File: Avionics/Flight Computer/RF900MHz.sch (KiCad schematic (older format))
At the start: 51 parts, among them J4 734120110, U1 CC1310F128RGZR, U2 CC1190RGVR, Y3 XRCGB24M000F2P00R0

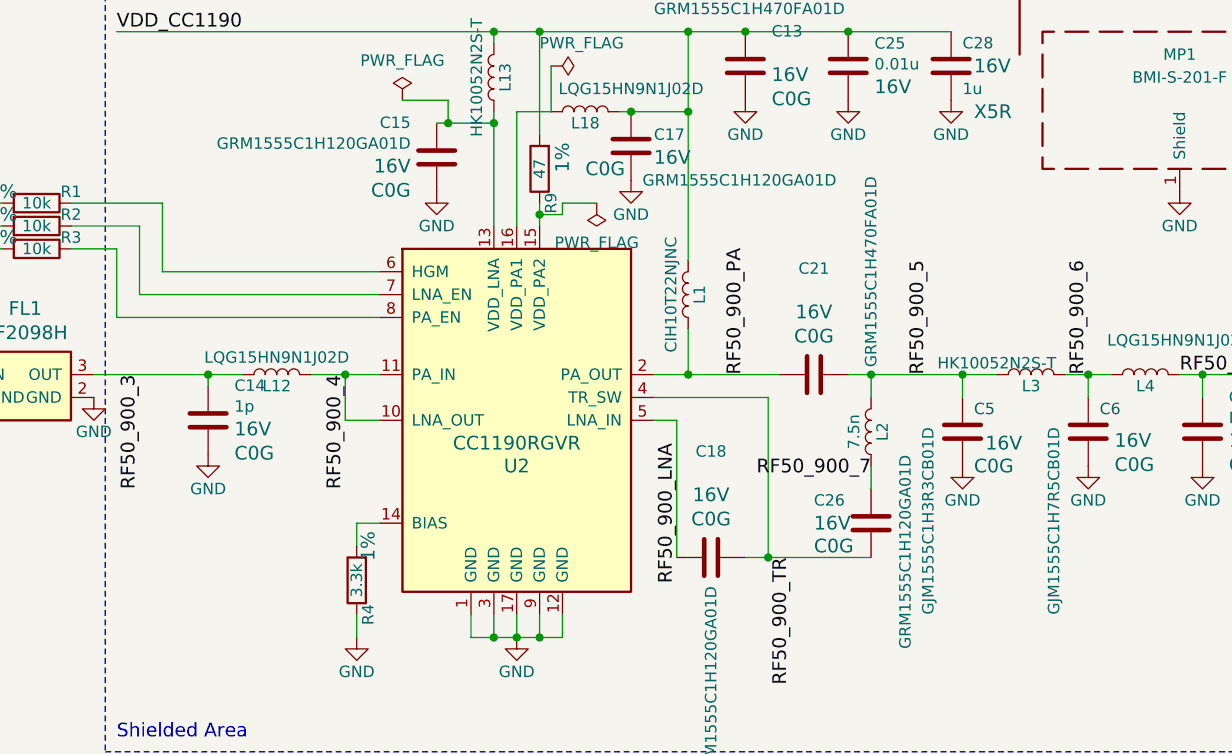
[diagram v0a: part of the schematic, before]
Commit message: Rebuilt output files and generated a few BOM fixes.
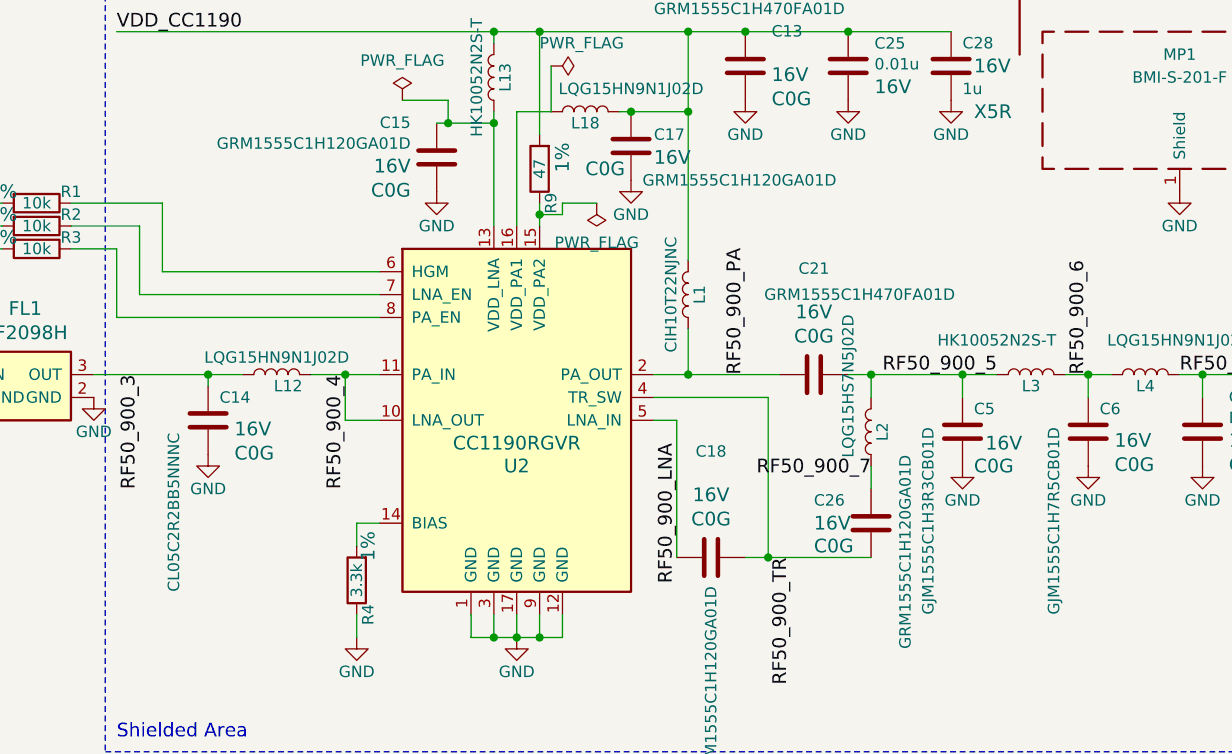
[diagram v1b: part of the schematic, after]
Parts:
- C14: value 1p -> CL05C2R2BB5NNNC
- L2: value 7.5n -> LQG15HS7N5J02D
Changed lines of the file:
@@
 P 8600 2550
 F 0 "L2" V 8550 2550 50  0000 C CNN
-F 1 "7.5n" V 8675 2550 50  0000 C CNN
+F 1 "LQG15HS7N5J02D" V 8700 2350 50  0000 C CNN
 F 2 "Inductors_SMD:L_0402" H 8600 2550 50  0001 C CNN
 F 3 "" H 8600 2550 50  0001 C CNN
@@
 P 9300 2300
 F 0 "L3" V 9250 2300 50  0000 C CNN
-F 1 "HK10052N2S-T" V 9350 2450 50  0000 C CNN
+F 1 "HK10052N2S-T" V 9450 2450 50  0000 C CNN
 F 2 "Inductors_SMD:L_0402" H 9300 2300 50  0001 C CNN
 F 3 "" H 9300 2300 50  0001 C CNN
@@
 U 1 1 58B31E99
 P 6000 2300
-F 0 "L12" V 5950 2300 50  0000 C CNN
+F 0 "L12" V 5950 2250 50  0000 C CNN
 F 1 "LQG15HN9N1J02D" V 6075 2300 50  0000 C CNN
 F 2 "Inductors_SMD:L_0402" H 6000 2300 50  0001 C CNN
@@
 U 1 1 58B4147C
 P 5700 2500
-F 0 "C14" H 5585 2348 50  0000 R CNN
-F 1 "1p" H 5585 2439 50  0000 R CNN
+F 0 "C14" H 5650 2400 50  0000 R CNN
+F 1 "CL05C2R2BB5NNNC" V 5850 3250 50  0000 R CNN
 F 2 "Capacitors_SMD:C_0402" H 988 1050 50  0001 C CNN
 F 3 "" H 950 1200 50  0001 C CNN
@@
 P 8350 2300
 F 0 "C21" V 8814 2300 50  0000 C CNN
-F 1 "GRM1555C1H470FA01D" H 8800 2050 50  0000 C CNN
+F 1 "GRM1555C1H470FA01D" V 8700 2100 50  0000 C CNN
 F 2 "Capacitors_SMD:C_0402" H 3638 850 50  0001 C CNN
 F 3 "" H 3600 1000 50  0001 C CNN
@@
 Text Label 8250 3100 3    60   ~ 0
 RF50_900_TR
-Text Label 8850 2300 1    60   ~ 0
+Text Label 8650 2300 0    60   ~ 0
 RF50_900_5
 Text Label 9550 2300 1    60   ~ 0

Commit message: Updated more manufacturing part numbers for macrofab compatibility.
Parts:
- D6: value LED-0603-RED -> MF-LED-0603-RED
- J4: value 734120110 -> 0734120110
- L15: value BLM18HE152SN1 -> BLM18HE152SN1D
- R4: value 3.3k -> RC0402FR-073K3L
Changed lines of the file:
@@
 P 10900 2300
 F 0 "J4" H 10910 2420 50  0000 C CNN
-F 1 "734120110" V 11015 2300 50  0000 C CNN
+F 1 "0734120110" V 11015 2300 50  0000 C CNN
 F 2 "Connectors_Molex:Molex_Microcoaxial_RF" H 10900 2300 50  0001 C CNN
 F 3 "http://www.molex.com/pdm_docs/sd/734120110_sd.pdf" H 10900 2300 50  0001 C CNN
@@
 P 6750 4800
 F 0 "L15" V 6700 4800 50  0000 C CNN
-F 1 "BLM18HE152SN1" V 6850 4700 50  0000 C CNN
+F 1 "BLM18HE152SN1D" V 6850 4700 50  0000 C CNN
 F 2 "Inductors_SMD:L_0603" H 6750 4800 50  0001 C CNN
 F 3 "" H 6750 4800 50  0001 C CNN
@@
 P 6350 3200
 F 0 "R4" V 6300 3350 50  0000 C CNN
-F 1 "3.3k" V 6350 3200 50  0000 C CNN
+F 1 "RC0402FR-073K3L" V 6500 3250 50  0000 C CNN
 F 2 "Resistors_SMD:R_0402" V 1450 2200 50  0001 C CNN
 F 3 "" V 1730 2200 50  0001 C CNN
@@
 P 6200 6750
 F 0 "D6" V 6300 6700 50  0000 R CNN
-F 1 "LED-0603-RED" H 6450 6850 50  0000 R CNN
+F 1 "MF-LED-0603-RED" H 6600 6850 50  0000 R CNN
 F 2 "LEDs:LED_0603" H 800 400 50  0001 C CNN
 F 3 "https://s3.amazonaws.com/devpublic1/datasheets/S_110_LTST-C190KRKT-369667.pdf" H 800 400 50  0001 C CNN

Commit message: Finished replacement and supply tuning
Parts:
- MP1: value BMI-S-201-F -> BMI-S-101; footprint Shielding_Cabinets:Laird_Technologies_BMI-S-201-F_13.66x12.70mm -> Shielding_Cabinets:Laird_Technologies_BMI-S-101_13.66x12.70mm
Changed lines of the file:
@@
 P 9950 1100
 F 0 "MP1" H 9950 1300 50  0000 C CNN
-F 1 "BMI-S-201-F" H 9950 1200 50  0000 C CNN
-F 2 "Shielding_Cabinets:Laird_Technologies_BMI-S-201-F_13.66x12.70mm" H 9950 1000 50  0001 C CNN
+F 1 "BMI-S-101" H 9950 1200 50  0000 C CNN
+F 2 "Shielding_Cabinets:Laird_Technologies_BMI-S-101_13.66x12.70mm" H 9950 1000 50  0001 C CNN
 F 3 "" H 9950 1000 50  0001 C CNN
 	1    9950 1100
